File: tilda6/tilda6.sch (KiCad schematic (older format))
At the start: 11 parts, among them J1 Conn_02x05_Odd_Even, J2 Conn_02x02_Odd_Even, J3 Conn_02x02_Odd_Even, J4 Conn_02x05_Odd_Even, P1 USB_C_Plug, SW1 SW_SPDT, SW2 SW_SPST, SW3 SW_SPST, U1 ESP32-S2-MINI-1-N4

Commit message: Add 3d models for buttons (thanks castawayc)
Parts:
- SW2, SW3: footprint Button_Switch_SMD:SW_SPST_B3U-3000P-B -> tilda6:sidebutton-1TS003B-1400-3500A-CT
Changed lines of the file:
@@
 F 0 "SW2" H 4400 4685 50  0000 C CNN
 F 1 "SW_SPST" H 4400 4594 50  0000 C CNN
-F 2 "Button_Switch_SMD:SW_SPST_B3U-3000P-B" H 4400 4450 50  0001 C CNN
+F 2 "tilda6:sidebutton-1TS003B-1400-3500A-CT" H 4400 4450 50  0001 C CNN
 F 3 "~" H 4400 4450 50  0001 C CNN
 	1    4400 4450
@@
 F 0 "SW3" H 4400 5035 50  0000 C CNN
 F 1 "SW_SPST" H 4400 4944 50  0000 C CNN
-F 2 "Button_Switch_SMD:SW_SPST_B3U-3000P-B" H 4400 4800 50  0001 C CNN
+F 2 "tilda6:sidebutton-1TS003B-1400-3500A-CT" H 4400 4800 50  0001 C CNN
 F 3 "~" H 4400 4800 50  0001 C CNN
 	1    4400 4800

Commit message: First full layout
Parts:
- removed J1, J4: Conn_02x05_Odd_Even, Connector_PinSocket_1.27mm:PinSocket_2x05_P1.27mm_Vertical_SMD, symbol Connector_Generic:Conn_02x05_Odd_Even
- added C1, C2, C3, C4, C5, C6, C7, C8: C, Capacitor_SMD:C_0603_1608Metric, symbol Device:C
- added J1: Conn_02x14_Odd_Even, Connector_PinSocket_1.27mm:PinSocket_2x14_P1.27mm_Vertical_SMD, symbol Connector_Generic:Conn_02x14_Odd_Even
- added L1: MHCHL201610A-2R2M-Q8A, Inductor_SMD:L_Taiyo-Yuden_MD-2020, symbol Device:L
- added Q1, Q3: LP0404N3T5G, Package_TO_SOT_SMD:SOT-883, symbol Transistor_FET:TP0610T
- added Q2: 2SK3019, Package_TO_SOT_SMD:SOT-416, symbol corelib:2SK3019
- added R1, R2: 5.1k, Resistor_SMD:R_0402_1005Metric, symbol Device:R
- added R10, R11, R4, R5, R6: 10k, Resistor_SMD:R_0402_1005Metric, symbol Device:R
- added R12: 1k, Resistor_SMD:R_0402_1005Metric, symbol Device:R
- added R3: 1M, Resistor_SMD:R_0402_1005Metric, symbol Device:R
- added R7: 100k, Resistor_SMD:R_0402_1005Metric, symbol Device:R
- added R8: 267k, Resistor_SMD:R_0402_1005Metric, symbol Device:R_Small
- added R9: 1.43M, Resistor_SMD:R_0402_1005Metric, symbol Device:R_Small
- added RN1: R_Pack04, Resistor_SMD:R_Array_Convex_4x0603, symbol Device:R_Pack04
- added U10: ESDU5V0H4, Package_TO_SOT_SMD:SOT-23-6, symbol Power_Protection:SRV05-4
- added U2: LTH7R., Package_TO_SOT_SMD:TSOT-23-5, symbol Battery_Management:LTC4054ES5-4.2
- added U3: QMA7981, Package_LGA:LGA-12_2x2mm_P0.5mm, symbol corelib:QMA7981
- added U4: A1006TL, tilda6:A1006TL, symbol tilda6:A1006TL
- added U5: ESP-PSRAM32, Package_SO:SOIC-8_3.9x4.9mm_P1.27mm, symbol Memory_RAM:ESP-PSRAM32
- added U6: QMC7983, tilda6:QMC7983, symbol tilda6:QMC7983
- added U7: MT3520B, Package_TO_SOT_SMD:SOT-23-5, symbol Regulator_Switching:TLV62568DBV
- added U8: SSP61CC3002MR, Package_TO_SOT_SMD:SOT-23, symbol tilda6:SSP61CC3002MR
- added U9: SN74LVC1G125DBVR, Package_TO_SOT_SMD:SOT-23-5, symbol tilda6:SN74LVC1G125DBVR
- D1: value WS2812B -> WS2812B-SIDE-A
- P1: footprint corelib:UTC009-C -> corelib:UTC009-C-vias
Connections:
- net labels added: 3V3, ACCL_INT, AUTH_WKUP, BTN1, BTN2, BTN3, CHARGE_DET, D+, D-, EN, G0, G1, G2, G3, IO0, JOYC, JOYD, JOYL, JOYR, JOYU, LCD_BL_EN, LCD_CLK, LCD_CS, LCD_DC, LCD_DIN, LCD_PWR_EN, LCD_RST, LEDDATA, LEDOUT, LED_PWR, PI2C_SCL, PI2C_SDA, PSRAMCLK, PSRAMCS, PSRAMD, PSRAMHD, PSRAMQ, PSRAMWP, SI2C_SCL, SI2C_SDA, UVLO, VBAT_IN, VBAT_SW, VBUS, VLED
- wire segments 2 -> 83
- no-connect marks 0 -> 16
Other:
- note added: "Addressable LED"
- note added: "Battery charge"
- note added: "Battery measure, button, and disconnect"
- note added: "Battery\nmonitor"
- note added: "Board to board\nconnectors"
- note added: "DC/DC"
- note added: "I2C sensors+auth"
- note added: "MCU module"
- note added: "PSRAM"
- note added: "USB connector"
- moved on the sheet: D1, J2, J3, N1, P1, SW1, SW2, SW3

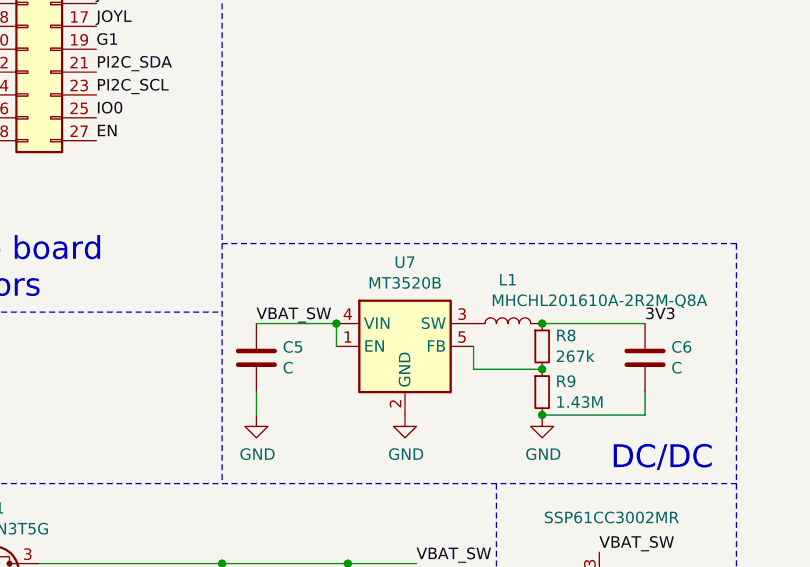
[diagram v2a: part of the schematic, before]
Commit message: Change DC/DC to M3406-ADJ for lower quiescent current at low load
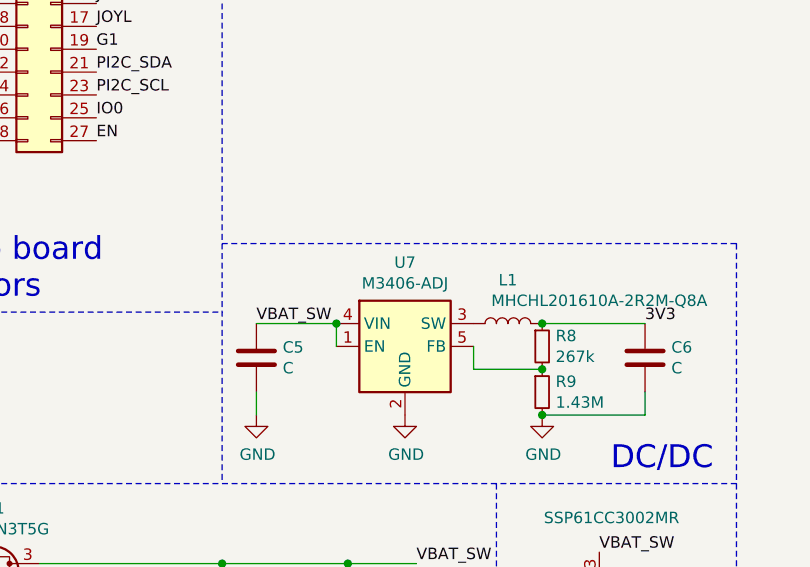
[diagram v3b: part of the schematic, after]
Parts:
- L1: footprint Inductor_SMD:L_Taiyo-Yuden_MD-2020 -> tilda6:MHCHL201610A-2R2M-Q8A
- U7: value MT3520B -> M3406-ADJ
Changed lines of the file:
@@
 P 5500 4100
 F 0 "U7" H 5500 4467 50  0000 C CNN
-F 1 "MT3520B" H 5500 4376 50  0000 C CNN
+F 1 "M3406-ADJ" H 5500 4376 50  0000 C CNN
 F 2 "Package_TO_SOT_SMD:SOT-23-5" H 5550 3850 50  0001 L CIN
 F 3 "http://www.ti.com/lit/ds/symlink/tlv62568.pdf" H 5250 4550 50  0001 C CNN
@@
 F 0 "L1" V 6140 4000 50  0000 C CNN
 F 1 "MHCHL201610A-2R2M-Q8A" V 6050 3600 50  0000 C CNN
-F 2 "Inductor_SMD:L_Taiyo-Yuden_MD-2020" H 5950 4000 50  0001 C CNN
+F 2 "tilda6:MHCHL201610A-2R2M-Q8A" H 5950 4000 50  0001 C CNN
 F 3 "~" H 5950 4000 50  0001 C CNN
 	1    5950 4000

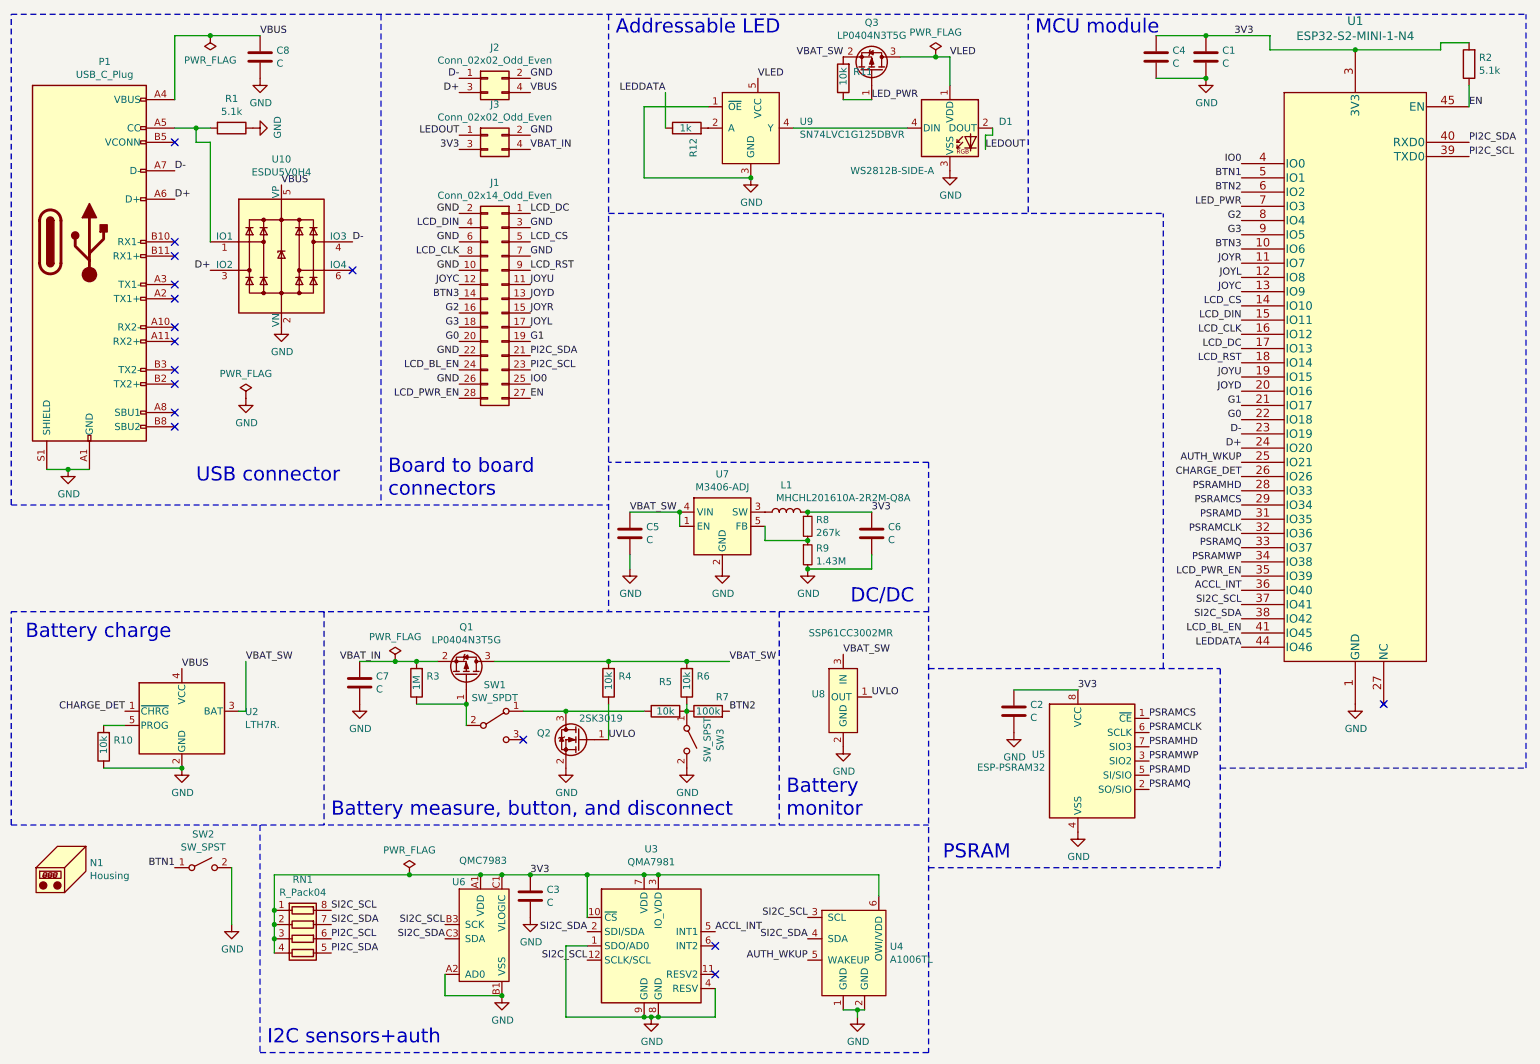
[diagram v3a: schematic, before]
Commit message: Implement most of martling's recommendations: - power switch now controls DC/DC enable - top board caps changed from 1x4.7u to 1x1u+1x10n - top board edge via stitching - bottom board ground all around edge where possible - changed UVLO monitor threshold to 3.3V - all outermost traces very close to edge are now gnd not implemented: VBUS ferrite
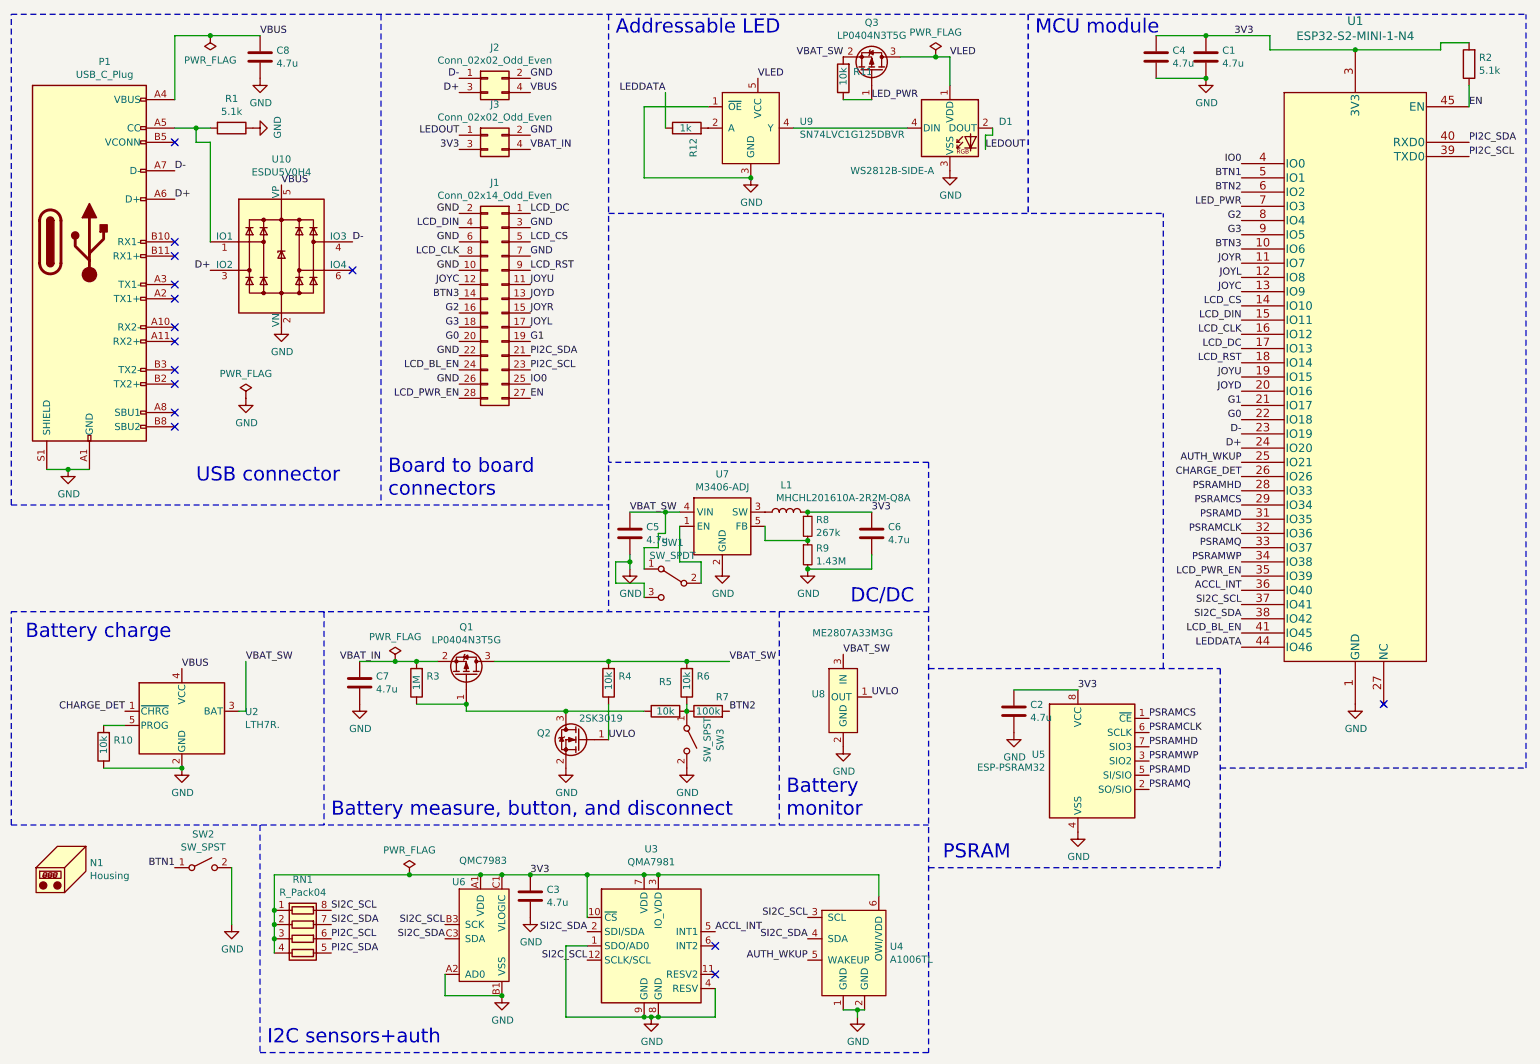
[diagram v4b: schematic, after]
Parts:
- C1, C2, C3, C4, C5, C6, C7, C8: value C -> 4.7u
- U8: value SSP61CC3002MR -> ME2807A33M3G
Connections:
- net GND: now also SW1.3 (C)
- net VBAT_SW: now also SW1.1 (A); no longer U7.1 (EN)
- net at Q2.3 (D), R5.1: now also Q1.1 (G), R3.1; no longer SW1.1 (A)
- new net: SW1.2 (B), U7.1 (EN)
- no-connect marks 16 -> 15
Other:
- moved on the sheet: SW1
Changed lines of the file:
@@
 L Switch:SW_SPDT SW1
 U 1 1 60FDC6A6
-P 3900 5500
-F 0 "SW1" H 3900 5785 50  0000 C CNN
-F 1 "SW_SPDT" H 3900 5694 50  0000 C CNN
-F 2 "Button_Switch_SMD:SW_SPDT_PCM12" H 3900 5500 50  0001 C CNN
-F 3 "~" H 3900 5500 50  0001 C CNN
-	1    3900 5500
-	1    0    0    -1
+P 5150 4500
+F 0 "SW1" H 5150 4785 50  0000 C CNN
+F 1 "SW_SPDT" H 5150 4694 50  0000 C CNN
+F 2 "Button_Switch_SMD:SW_SPDT_PCM12" H 5150 4500 50  0001 C CNN
+F 3 "~" H 5150 4500 50  0001 C CNN
+	1    5150 4500
+	-1   0    0    -1
 $EndComp
 $Comp
@@
 P 8900 800
 F 0 "C1" H 9015 846 50  0000 L CNN
-F 1 "C" H 9015 755 50  0000 L CNN
+F 1 "4.7u" H 9015 755 50  0000 L CNN
 F 2 "Capacitor_SMD:C_0603_1608Metric" H 8938 650 50  0001 C CNN
 F 3 "~" H 8900 800 50  0001 C CNN
@@
 P 7550 5400
 F 0 "C2" H 7665 5446 50  0000 L CNN
-F 1 "C" H 7665 5355 50  0000 L CNN
+F 1 "4.7u" H 7665 5355 50  0000 L CNN
 F 2 "Capacitor_SMD:C_0603_1608Metric" H 7588 5250 50  0001 C CNN
 F 3 "~" H 7550 5400 50  0001 C CNN
@@
 P 4150 6700
 F 0 "C3" H 4265 6746 50  0000 L CNN
-F 1 "C" H 4265 6655 50  0000 L CNN
+F 1 "4.7u" H 4265 6655 50  0000 L CNN
 F 2 "Capacitor_SMD:C_0603_1608Metric" H 4188 6550 50  0001 C CNN
 F 3 "~" H 4150 6700 50  0001 C CNN
@@
 P 8550 800
 F 0 "C4" H 8665 846 50  0000 L CNN
-F 1 "C" H 8665 755 50  0000 L CNN
+F 1 "4.7u" H 8665 755 50  0000 L CNN
 F 2 "Capacitor_SMD:C_0603_1608Metric" H 8588 650 50  0001 C CNN
 F 3 "~" H 8550 800 50  0001 C CNN
@@
 $EndComp
 Wire Wire Line
-	3700 5350 3700 5500
+	3700 5350 3700 5400
 Connection ~ 3700 5350
-NoConn ~ 4100 5600
-Wire Wire Line
-	4400 5400 4100 5400
 Text Label 5550 5050 0    50   ~ 0
 VBAT_SW
@@
 	1    0    0    -1
 $EndComp
-Wire Wire Line
-	4700 5050 5250 5050
 $Comp
 L Device:R R6
@@
 	5250 5350 5250 5400
 $Comp
-L Regulator_Switching:TLV62568DBV U7
-U 1 1 62186CE2
-P 5500 4100
-F 0 "U7" H 5500 4467 50  0000 C CNN
-F 1 "M3406-ADJ" H 5500 4376 50  0000 C CNN
-F 2 "Package_TO_SOT_SMD:SOT-23-5" H 5550 3850 50  0001 L CIN
-F 3 "http://www.ti.com/lit/ds/symlink/tlv62568.pdf" H 5250 4550 50  0001 C CNN
-	1    5500 4100
-	1    0    0    -1
-$EndComp
-$Comp
 L power:GND #PWR05
 U 1 1 621896D7
@@
 P 6550 4150
 F 0 "C6" H 6665 4196 50  0000 L CNN
-F 1 "C" H 6665 4105 50  0000 L CNN
+F 1 "4.7u" H 6665 4105 50  0000 L CNN
 F 2 "Capacitor_SMD:C_0603_1608Metric" H 6588 4000 50  0001 C CNN
 F 3 "~" H 6550 4150 50  0001 C CNN
@@
 P 4850 4150
 F 0 "C5" H 4965 4196 50  0000 L CNN
-F 1 "C" H 4965 4105 50  0000 L CNN
+F 1 "4.7u" H 4965 4105 50  0000 L CNN
 F 2 "Capacitor_SMD:C_0603_1608Metric" H 4888 4000 50  0001 C CNN
 F 3 "~" H 4850 4150 50  0001 C CNN
@@
 $EndComp
 Wire Wire Line
-	5200 4000 4850 4000
-Wire Wire Line
-	5200 4100 5200 4000
-Connection ~ 5200 4000
+	5200 4000 5100 4000
 $Comp
 L power:GND #PWR04
@@
 $EndComp
 Wire Wire Line
-	4850 4400 4850 4300
+	4850 4400 4850 4350
 Text Label 4850 4000 0    50   ~ 0
 VBAT_SW
@@
 P 2950 5200
 F 0 "C7" H 3065 5246 50  0000 L CNN
-F 1 "C" H 3065 5155 50  0000 L CNN
+F 1 "4.7u" H 3065 5155 50  0000 L CNN
 F 2 "Capacitor_SMD:C_0603_1608Metric" H 2988 5050 50  0001 C CNN
 F 3 "~" H 2950 5200 50  0001 C CNN
@@
 P 2250 800
 F 0 "C8" H 2365 846 50  0000 L CNN
-F 1 "C" H 2365 755 50  0000 L CNN
+F 1 "4.7u" H 2365 755 50  0000 L CNN
 F 2 "Capacitor_SMD:C_0603_1608Metric" H 2288 650 50  0001 C CNN
 F 3 "~" H 2250 800 50  0001 C CNN
@@
 P 6350 5300
 F 0 "U8" H 6222 5321 50  0000 R CNN
-F 1 "SSP61CC3002MR" H 6700 5750 50  0000 R CNN
+F 1 "ME2807A33M3G" H 6700 5750 50  0000 R CNN
 F 2 "Package_TO_SOT_SMD:SOT-23" H 6350 5300 50  0001 C CNN
 F 3 "" H 6350 5300 50  0001 C CNN
@@
 	1    0    0    -1
 $EndComp
+Wire Wire Line
+	3700 5400 4400 5400
+$Comp
+L Regulator_Switching:TLV62568DBV U7
+U 1 1 62186CE2
+P 5500 4100
+F 0 "U7" H 5500 4467 50  0000 C CNN
+F 1 "M3406-ADJ" H 5500 4376 50  0000 C CNN
+F 2 "Package_TO_SOT_SMD:SOT-23-5" H 5550 3850 50  0001 L CIN
+F 3 "http://www.ti.com/lit/ds/symlink/tlv62568.pdf" H 5250 4550 50  0001 C CNN
+	1    5500 4100
+	1    0    0    -1
+$EndComp
+Wire Wire Line
+	4700 5050 5250 5050
+Wire Wire Line
+	4950 4400 4950 4250
+Wire Wire Line
+	4950 4250 5050 4250
+Wire Wire Line
+	5050 4250 5050 4150
+Wire Wire Line
+	5050 4150 5100 4150
+Wire Wire Line
+	5100 4150 5100 4000
+Connection ~ 5100 4000
+Wire Wire Line
+	5100 4000 4850 4000
+Wire Wire Line
+	5350 4500 5350 4350
+Wire Wire Line
+	5350 4350 5200 4350
+Wire Wire Line
+	5200 4350 5200 4100
+Wire Wire Line
+	4950 4600 4950 4500
+Wire Wire Line
+	4950 4500 4750 4500
+Wire Wire Line
+	4750 4500 4750 4350
+Wire Wire Line
+	4750 4350 4850 4350
+Connection ~ 4850 4350
+Wire Wire Line
+	4850 4350 4850 4300
 $EndSCHEMATC
